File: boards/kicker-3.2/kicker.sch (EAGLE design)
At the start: 151 parts, among them J1 B2PS-VH(LF)(SN), J2 HFW8R-1ST, J3 B2PS-VH(LF)(SN), J4 B2PS-VH(LF)(SN), J5 2-PIN_2MM-H, J6 3-PIN_2MM-H, J7 !BTN_KCK_PRE_EXT, J8 !BTN_CHP_PRE_EXT, J9 !BTN_CHG_PRE_EXT, Q1 ATP302ATPAK, Q10 BSS806NSOT-23-3, Q2 IRFS4227, Q3 BSS127, Q4 BSS127, Q5 BSS127, Q6 BSS127, Q7 AOD1N60, T1 DA203X-ALDA2034, U1 MPM3620GQV-P, U2 15V, U3 LT3751FE, U4 AT32ATQFP44, U5 IX4427N, U6 MAX6817, U7 MAX6817

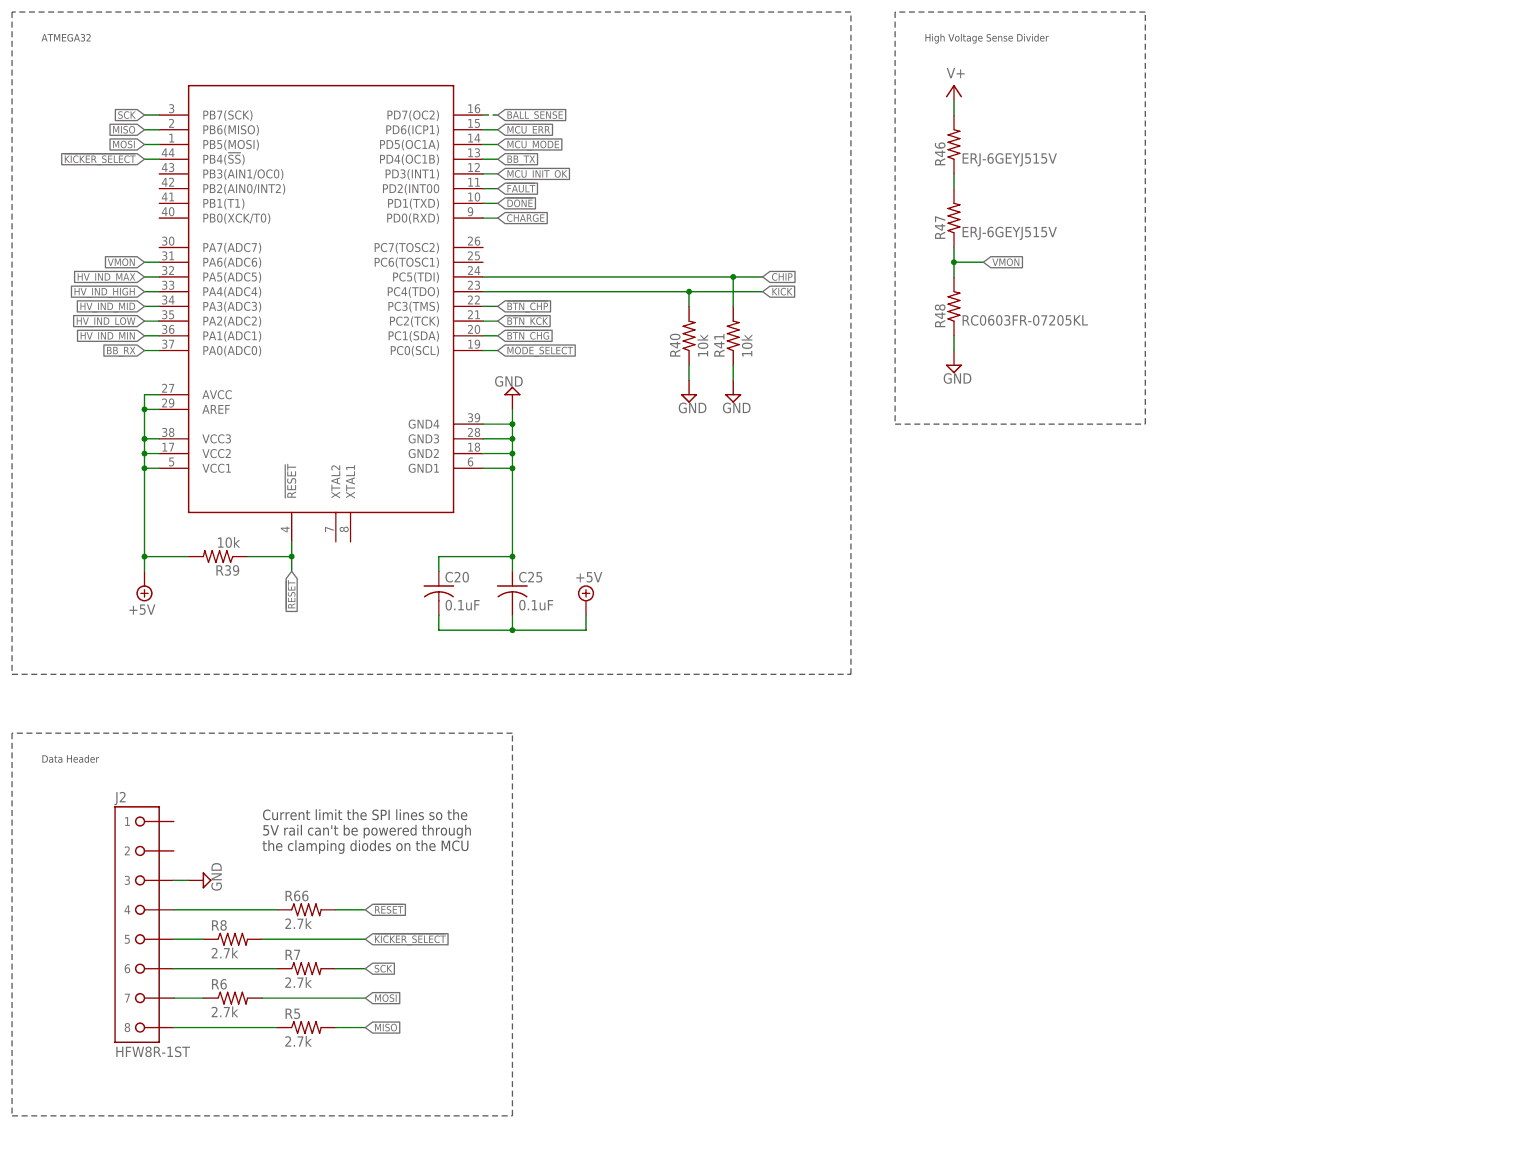
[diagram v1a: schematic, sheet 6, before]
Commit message: kicker passing initial drc checks
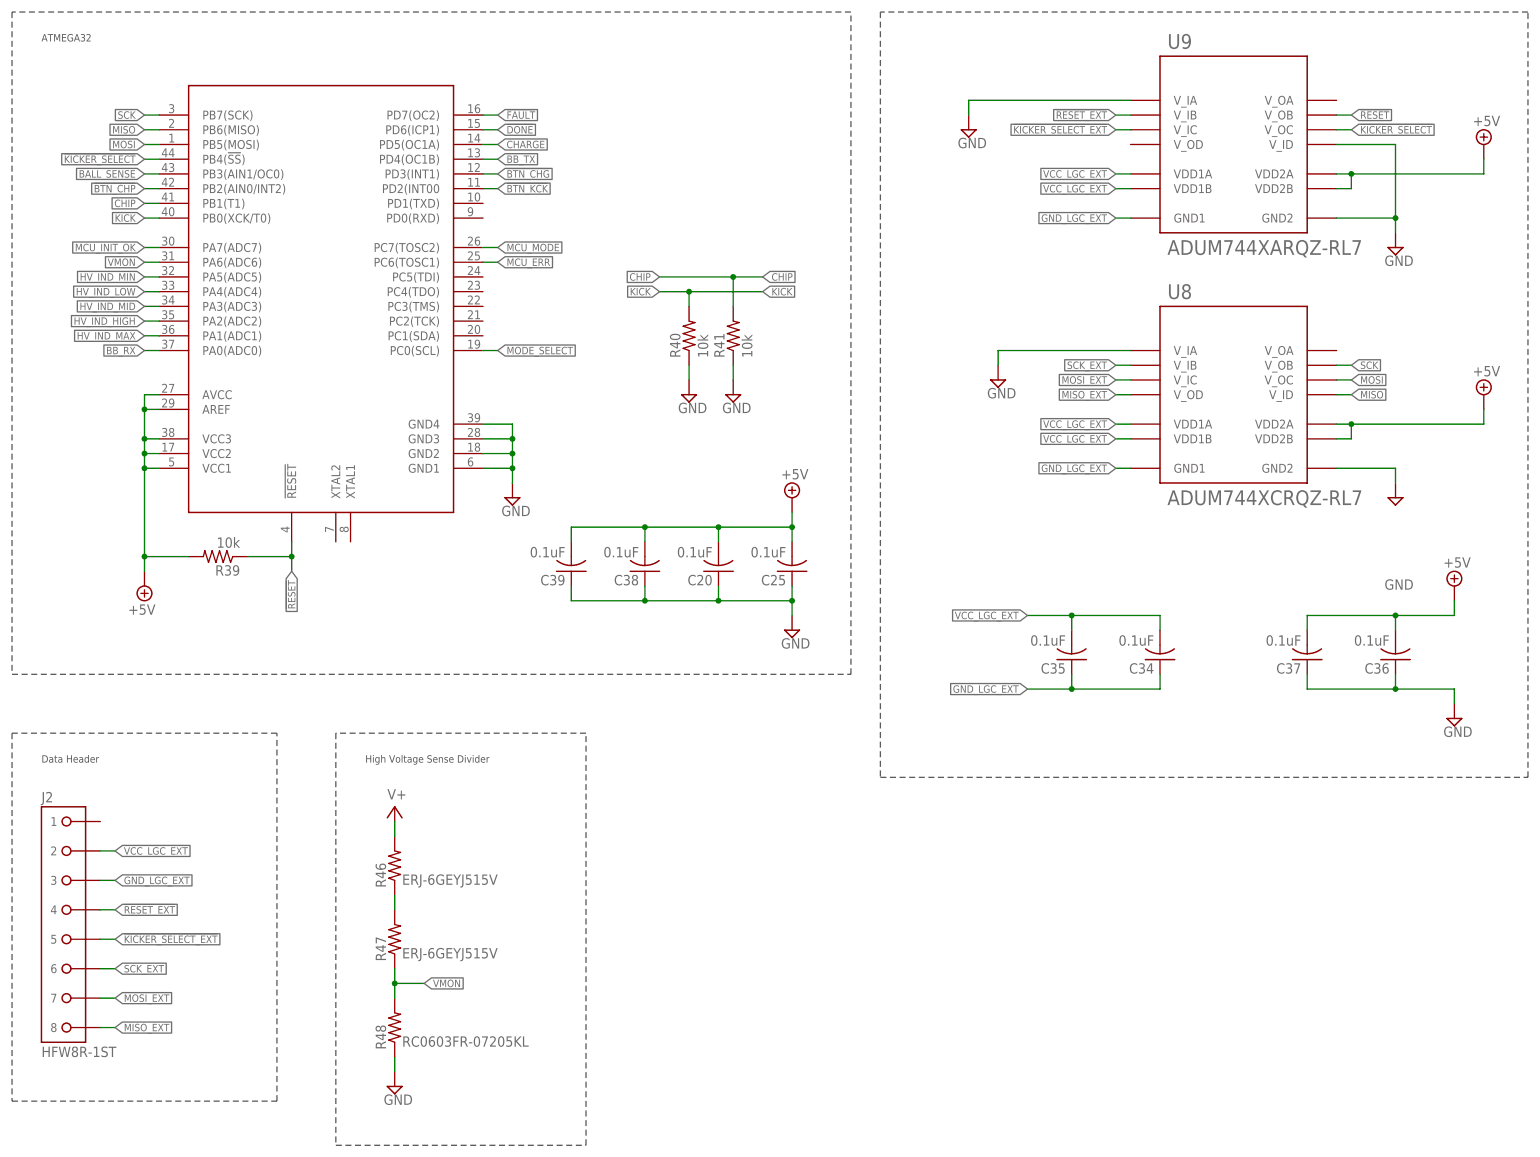
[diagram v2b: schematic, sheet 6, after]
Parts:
- removed R21, R23, R32: 162, rcl:R-US_R0603
- removed R25, R27, R29, R33: 261, rcl:R-US_R0603
- removed R5, R6, R66, R7, R8: 2.7k, resistor:R-US_R0603
- removed R55: 60, rcl:R-US_R0603
- removed U6, U7: MAX6817, RoboJackets-ICs:MAX6817
- added C34, C35, C36, C37, C38, C39: 0.1uF, rcl:C-USC0603
- added RN1: 330, RoboJackets-Resistors:RA-8
- added RV1: 500, RoboJackets-Resistors:PVG3
- added U8: ADUM744XCRQZ-RL7, RoboJackets-ICs:ADUM744XCRQZ-RL7
- added U9: ADUM744XARQZ-RL7, RoboJackets-ICs:ADUM744XARQZ-RL7
- R22, R24: value 162 -> 330
- R28: value 261 -> 330
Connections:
- removed net !BTN_CHG_PRE: J9.1, R53.1, S3.A2, U7.IN2
- removed net !BTN_CHP_PRE: J8.1, R52.1, S2.A2, U6.IN2
- removed net !BTN_KCK_PRE: J7.1, R54.1, S4.A2, U6.IN1
- removed net !KICKER_SELECT_CL: J2G$1.5, R8.1
- removed net !RESET_CL: J2G$1.4, R66.1
- removed net MISO_CL: J2G$1.8, R5.1
- removed net MOSI_CL: J2G$1.7, R6.1
- removed net N$11: D3.A, R21.1
- removed net N$12: D5.A, R23.1
- removed net N$13: D7.A, R25.1
- removed net N$17: D20.A, R55.1
- removed net N$21: D8.A, R27.1
- removed net N$30: D10.A, R29.1
- removed net N$4: D13.A, R32.1
- removed net N$40: D12.A, R31.1
- removed net SCK_CL: J2G$1.6, R7.1
- new net !KICKER_SELECT_EXT: J2G$1.5, U9.V_IC
- new net !RESET_EXT: J2G$1.4, U9.V_IB
- new net BALL_SENSE_CL: D12.K, R31.1
- new net GND_LGC_EXT: C34.1, C35.1, J2G$1.3, U8.GND1, U9.GND1
- new net HV_IND_HIGH_CL: D8.K, RN1.7
- new net HV_IND_LOW_CL: D5.K, RN1.5
- new net HV_IND_MAX_CL: D10.K, RN1.8
- new net HV_IND_MID_CL: D7.K, RN1.6
- new net HV_IND_MIN_CL: D3.K, RN1.4
- new net MCU_ERR_CL: D14.K, RN1.1
- new net MCU_INIT_OK_CL: D13.K, RN1.3
- new net MCU_MODE_CL: D20.K, RN1.2
- new net MISO_EXT: J2G$1.8, U8.V_OD
- new net MOSI_EXT: J2G$1.7, U8.V_IC
- new net N$2: U8.V_IA
- new net SCK_EXT: J2G$1.6, U8.V_IB
- new net VCC_LGC_EXT: C34.2, C35.2, J2G$1.2, U8.VDD1A, U8.VDD1B, U9.VDD1A, U9.VDD1B
- net !BTN_CHG: now also J9.1, R53.1, S3.A2, U4.PD3(INT1); no longer U4.PC1(SDA), U7.OUT2
- net !BTN_CHP: now also J8.1, R52.1, S2.A2, U4.PB2(AIN0/INT2); no longer U4.PC3(TMS), U6.OUT2
- net !BTN_KCK: now also J7.1, R54.1, S4.A2, U4.PD2(INT00; no longer U4.PC2(TCK), U6.OUT1
- net !DONE!: now also U4.PD6(ICP1); no longer U4.PD1(TXD)
- net !FAULT!: now also U4.PD7(OC2); no longer U4.PD2(INT00
- net !KICKER_SELECT: now also U9.V_OC; no longer R8.2
- net !RESET: now also U9.V_OB; no longer R66.2
- net +5V: now also C36.2, C37.2, C38.2, C39.2, D10.A, D12.A, D13.A, D14.A, D20.A, D3.A, D5.A, D7.A, D8.A, RV1.PIN2, U8.VDD2A, U8.VDD2B, U9.VDD2A, U9.VDD2B; no longer R21.2, R23.2, R25.2, R27.2, R29.2, R31.2, R32.2, R33.2, R49.1, R55.2, U6.VCC, U7.VCC
- net BALL_SENSE: now also R31.2, U4.PB3(AIN1/OC0); no longer D12.K, U4.PD7(OC2)
- net CHARGE: now also U4.PD5(OC1A); no longer U4.PD0(RXD)
- net CHIP: now also U4.PB1(T1); no longer U4.PC5(TDI)
- net GND: now also C36.1, C37.1, C38.1, C39.1, U8.GND2, U9.GND2, U9.V_IA, U9.V_ID; no longer J2G$1.3, U6.GND, U7.GND
- net HV_IND_HIGH: now also RN1.10, U4.PA2(ADC2); no longer D8.K, U4.PA4(ADC4)
- net HV_IND_LOW: now also RN1.12, U4.PA4(ADC4); no longer D5.K, U4.PA2(ADC2)
- net HV_IND_MAX: now also RN1.9, U4.PA1(ADC1); no longer D10.K, U4.PA5(ADC5)
- net HV_IND_MID: now also RN1.11; no longer D7.K
- net HV_IND_MIN: now also RN1.13, U4.PA5(ADC5); no longer D3.K, U4.PA1(ADC1)
- net KICK: now also U4.PB0(XCK/T0); no longer U4.PC4(TDO)
- net MCU_ERR: now also RN1.16, U4.PC6(TOSC1); no longer D14.K, U4.PD6(ICP1)
- net MCU_INIT_OK: now also RN1.14, U4.PA7(ADC7); no longer D13.K, U4.PD3(INT1)
- net MCU_MODE: now also RN1.15, U4.PC7(TOSC2); no longer D20.K, U4.PD5(OC1A)
- net MISO: now also U8.V_ID; no longer R5.2
- net MOSI: now also U8.V_OC; no longer R6.2
- net N$3: now also R49.1, RV1.PIN3; no longer D14.A, R33.1
- net SCK: now also U8.V_OB; no longer R7.2
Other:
- note removed: "Charge Switch"
- note removed: "Current limit the SPI lines so the 5V rail can't be powered through the clamping diodes on the MCU"
- note removed: "MCU Status"
- note removed: "Mode"
- moved on the sheet: C20, C25, D10, D12, D13, D14, D20, D3, D5, D7, D8, J2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

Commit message: updated LT calibration, added docs for LT
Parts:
- removed D24: PTVS20VS1UR, RoboJackets-Diodes:TVSSOD123W
- removed R53, R54: 10k, rcl:R-US_R0603
- removed R56: 22, resistor:R-US_R0805
- removed R57: 100k, rcl:R-US_R0603
- removed R59: 100k, rcl:R-US_R0402
- removed R60: 43.2k, rcl:R-US_R0603
- removed R61: 160k 1%, rcl:R-US_R0402
- removed R62: 30.1k 1%, rcl:R-US_R0402
- removed R64: 931, rcl:R-US_R0805
- removed R65: 160, rcl:R-US_R0603
- removed U$6, U$7: IXGK400N30A3, RoboJackets-Discrete:IXGK400N30A3
- added D21: BLUE, RoboJackets-LEDs:LED-SMD-BLUE
- added Q8, Q9: BSS127, RoboJackets-Discrete:BSS127
- added R23: 100k, rcl:R-US_R0603
- added R25: 10k, rcl:R-US_R0603
- added R27: 160, rcl:R-US_R1206
- added R29: 270k, rcl:R-US_R0603
- added R32: ERJ-6GEYJ515V, rcl:R-US_R0805
- added R33: 1.5k 35W, RoboJackets-Resistors:PWR263S-35TO-263AB
- added R5: 110k 1%, resistor:R-US_R0603
- added R6: 10k 1%, resistor:R-US_R0603
- added R7: 294k 1%, resistor:R-US_R0805
- added R8: 412k 1%, resistor:R-US_R0805
- C11: value 560uF -> 10uF (X7R); device rcl:CPOL-USE7.5-18 -> rcl:C-USC1210
- C12: value 1000uF -> 10uF (X7R); device rcl:CPOL-USE10-25 -> rcl:C-USC1210
- C13, C27: value 0.1uF -> 10uF (X7R); device rcl:C-USC0603 -> rcl:C-USC1210
- C14: value 1000uF -> 0.1uF; device rcl:CPOL-USE10-25 -> rcl:C-USC0603
- C15: value 10pF -> 0.1uF; device resistor:C-USC0603 -> rcl:C-USC0603
- C16, C32, C33: value 10uF (X7R) -> 0.1uF; device rcl:C-USC1210 -> rcl:C-USC0603
- C17, C18: value 10uF (X7R) -> 10pF; device rcl:C-USC1210 -> resistor:C-USC0603
- C19: value 10uF (X7R) -> 1uF; device rcl:C-USC1210 -> rcl:C-USC0603
- C20, C25: value 0.1uF -> 1uF
- C21: value 0.1uF 35V -> 560uF; device rcl:C-USC0603 -> rcl:CPOL-USE7.5-18
- C22: value 22uF 35V -> 10uF (X7R); device rcl:C-USC0805 -> rcl:C-USC1210
- C23, C24: value 0.1uF 50V -> 10uF (X7R); device rcl:C-USC0603 -> rcl:C-USC1210
- C26: value 220pF 100V -> 10uF (X7R); device resistor:C-USC0805 -> rcl:C-USC1210
- C28: value 0.1uF -> 0.1uF 35V
- C29: value 10pF -> 22uF 35V; device resistor:C-USC0603 -> rcl:C-USC0805
- C30, C31: value 10uF (X7R) -> 0.1uF 50V; device rcl:C-USC1210 -> rcl:C-USC0603
- C4: value 1uF -> 2.2uF
- C5: value 1uF -> 1000uF; device rcl:C-USC0603 -> rcl:CPOL-USE10-25
- C6: value 2.2uF -> 1000uF; device rcl:C-USC0603 -> rcl:CPOL-USE10-25
- C9: value 1uF -> 220pF 100V; device rcl:C-USC0603 -> resistor:C-USC0805
- D1: value VS-5EWH06FN-M3D-PAK_TO252AA -> PTVS20VS1UR; device RoboJackets-Diodes:VS-5EWH06FN-M3D-PAK_TO252AA -> RoboJackets-Diodes:TVSSOD123W
- D10, D8: value RED -> GREEN; device RoboJackets-LEDs:LED-SMD-RED -> RoboJackets-LEDs:LED-SMD-GREEN
- D11: value YELLOW -> RED; device RoboJackets-LEDs:LED-SMD-YELLOW -> RoboJackets-LEDs:LED-SMD-RED
- D12: value BLUE -> YELLOW; device RoboJackets-LEDs:LED-SMD-BLUE -> RoboJackets-LEDs:LED-SMD-YELLOW
- D13: value GREEN -> YELLOW; device RoboJackets-LEDs:LED-SMD-GREEN -> RoboJackets-LEDs:LED-SMD-YELLOW
- D14: value RED -> BLUE; device RoboJackets-LEDs:LED-SMD-RED -> RoboJackets-LEDs:LED-SMD-BLUE
- D15: value 3SMBJ5929B-TP -> GREEN; device RoboJackets-Diodes:DIODE-DO214AA -> RoboJackets-LEDs:LED-SMD-GREEN
- D16: value SMAJ20ADO-214AC -> GREEN; device RoboJackets-Diodes:SMAJ20ADO-214AC -> RoboJackets-LEDs:LED-SMD-GREEN
- D17: value SMAJ20ADO-214AC -> YELLOW; device RoboJackets-Diodes:SMAJ20ADO-214AC -> RoboJackets-LEDs:LED-SMD-YELLOW
- D18, D19: value VS-5EWH06FN-M3D-PAK_TO252AA -> RED; device RoboJackets-Diodes:VS-5EWH06FN-M3D-PAK_TO252AA -> RoboJackets-LEDs:LED-SMD-RED
- D2, D6: value GREEN -> VS-5EWH06FN-M3D-PAK_TO252AA; device RoboJackets-LEDs:LED-SMD-GREEN -> RoboJackets-Diodes:VS-5EWH06FN-M3D-PAK_TO252AA
- D3: value BLUE -> SMAJ20ADO-214AC; device RoboJackets-LEDs:LED-SMD-BLUE -> RoboJackets-Diodes:SMAJ20ADO-214AC
- D4: value GREEN -> SMAJ20ADO-214AC; device RoboJackets-LEDs:LED-SMD-GREEN -> RoboJackets-Diodes:SMAJ20ADO-214AC
- D5: value YELLOW -> VS-5EWH06FN-M3D-PAK_TO252AA; device RoboJackets-LEDs:LED-SMD-YELLOW -> RoboJackets-Diodes:VS-5EWH06FN-M3D-PAK_TO252AA
- D7: value YELLOW -> 3SMBJ5929B-TP; device RoboJackets-LEDs:LED-SMD-YELLOW -> RoboJackets-Diodes:DIODE-DO214AA
- J2: value HFW8R-1ST -> B2PS-VH(LF)(SN); device RoboJackets-Connectors:HFW8R-1ST -> RoboJackets-Connectors:B2PS-VH(LF)(SN)
- J4: value B2PS-VH(LF)(SN) -> HFW8R-1ST; device RoboJackets-Connectors:B2PS-VH(LF)(SN) -> RoboJackets-Connectors:HFW8R-1ST
- Q3, Q4: value BSS127 -> IXGK400N30A3; device RoboJackets-Discrete:BSS127 -> RoboJackets-Discrete:IXGK400N30A3
- Q6: value BSS127 -> AOD1N60; device RoboJackets-Discrete:BSS127 -> RoboJackets-Discrete:AOD1N60
- Q7: value AOD1N60 -> BSS127; device RoboJackets-Discrete:AOD1N60 -> RoboJackets-Discrete:BSS127
- R1: value 110k 1% -> 43.2k; device resistor:R-US_R0603 -> rcl:R-US_R0603
- R11: value 294k 1% -> 25,5k 1%
- R12: value 412k 1% -> 1.00k 1%
- R13: value 40.2k 1% -> 11.5k 1%
- R14: value 1.62k 1% -> 25.5k 1%
- R15: value 18.2k 1% -> 22
- R16: value 40.2k 1% -> 15m 1%; device resistor:R-US_R0805 -> resistor:R-US_R2512
- R18: value 15m 1% -> 931; device resistor:R-US_R2512 -> rcl:R-US_R0805
- R2: value 10k 1% -> 100k; device resistor:R-US_R0603 -> rcl:R-US_R0402
- R20: value 1k -> 100k
- R22, R24: value 330 -> 160
- R26: value 1k -> 10k
- R28: value 330 -> 160; device rcl:R-US_R0603 -> rcl:R-US_R1206
- R3: value 160 -> 160k 1%; device rcl:R-US_R0603 -> rcl:R-US_R0402
- R30: value ERJ-P06J274V -> 100k; device rcl:R-US_R0805 -> rcl:R-US_R0603
- R31: value 60 -> ERJ-6GEYJ515V; device rcl:R-US_R0603 -> rcl:R-US_R0805
- R34: value 270k -> 10k
- R35: value 100k -> ERJ-6GEYJ515V; device rcl:R-US_R0603 -> rcl:R-US_R0805
- R37: value ERJ-6GEYJ515V -> RC0603FR-07205KL; device rcl:R-US_R0805 -> rcl:R-US_R0603
- R38: value 1.5k 35W -> 10k; device RoboJackets-Resistors:PWR263S-35TO-263AB -> rcl:R-US_R0603
- R4: value 100k -> 30.1k 1%; device rcl:R-US_R0603 -> rcl:R-US_R0402
- R40, R43: value 10k -> 1k
- R41, R42: value 10k -> 330
- R44: value 160 -> 330; device rcl:R-US_R1206 -> rcl:R-US_R0603
- R45: value 160 -> ERJ-P06J274V; device rcl:R-US_R1206 -> rcl:R-US_R0805
- R46: value ERJ-6GEYJ515V -> 60; device rcl:R-US_R0805 -> rcl:R-US_R0603
- R47: value ERJ-6GEYJ515V -> 50; device rcl:R-US_R0805 -> rcl:R-US_R0603
- R48: value RC0603FR-07205KL -> 10k
- R49: value 50 -> 10k
- U4: value AT32ATQFP44 -> IX4427N; device RoboJackets-ICs:AT32ATQFP44 -> RoboJackets-PowerICs:IX4427N
- U5: value IX4427N -> AT32ATQFP44; device RoboJackets-PowerICs:IX4427N -> RoboJackets-ICs:AT32ATQFP44
- XF1: value 30A -> 20A
- renumbered R58 to R21, R63 to R17, U8 to U7, U9 to U6
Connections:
- net !BTN_CHG: now also R52.1, S4.A2, U5.PD3(INT1); no longer R53.1, S3.A2, U4.PD3(INT1)
- net !BTN_CHP: now also R50.1, U5.PB2(AIN0/INT2); no longer R52.1, U4.PB2(AIN0/INT2)
- net !BTN_KCK: now also R51.1, S3.A2, U5.PD2(INT00; no longer R54.1, S4.A2, U4.PD2(INT00
- net !DONE!: now also C19.1, U5.PD6(ICP1); no longer C4.1, U4.PD6(ICP1)
- net !DONE!_RAW: now also Q7.G; no longer Q3.G
- net !FAULT!: now also C20.1, R22.1, U5.PD7(OC2); no longer C3.1, R65.1, U4.PD7(OC2)
- net !FAULT!_RAW: now also Q8.G, R20.1, R22.2; no longer Q4.G, R57.1, R65.2
- net !KICKER_SELECT: now also U5.PB4(!SS!); no longer U4.PB4(!SS!)
- net !KICKER_SELECT_EXT: now also J4G$1.5; no longer J2G$1.5
- net !RESET: now also R34.1, U5.!RESET!; no longer R39.1, U4.!RESET!
- net !RESET_EXT: now also J4G$1.4; no longer J2G$1.4
- net +15.0V: now also C28.2, C29.2, C4.1, R40.2, R5.2, U4.VDD; no longer C21.2, C22.2, C6.1, R1.2, R20.2, U5.VDD
- net +5V: now also C32.2, C33.2, C34.2, C35.2, D11.A, D16.A, D17.A, D18.A, D21.A, D9.A, R20.2, R3.2, R34.2, R41.2, R42.2, R43.2, R44.2, R48.2, R51.2, U5.AREF, U5.AVCC, U5.VCC1, U5.VCC2, U5.VCC3; no longer C20.2, C25.2, C36.2, C37.2, D10.A, D20.A, D3.A, D5.A, D7.A, D8.A, R22.2, R24.2, R26.2, R28.2, R39.2, R53.2, R54.2, R57.2, R61.2, U4.AREF, U4.AVCC, U4.VCC1, U4.VCC2, U4.VCC3
- net 15V_PWR_BR: now also D8.A, R40.1; no longer D2.A, R20.1
- net BALL_SENSE: now also R46.2, U5.PB3(AIN1/OC0); no longer R31.2, U4.PB3(AIN1/OC0)
- net BALL_SENSE_CL: now also D21.K, R46.1; no longer D12.K, R31.1
- net BB_RX: now also R48.1, U5.PA0(ADC0); no longer R50.1, U4.PA0(ADC0)
- net BB_TX: now also U5.PD4(OC1B); no longer U4.PD4(OC1B)
- net BB_TX_CL: now also R47.2; no longer R49.2
- net CHARGE: now also C25.1, R24.1, U5.PD5(OC1A); no longer C9.1, R3.1, U4.PD5(OC1A)
- net CHARGE_RAW: now also R23.2, R24.2; no longer R3.2, R4.2
- net CHIP: now also R39.2, U4.IN_A, U5.PB1(T1); no longer R41.2, U4.PB1(T1), U5.IN_A
- net CHIPPER: now also D5.A, J2.2, Q3.C; no longer D18.A, J3.2, U$7.C
- net CHIP_GATE: now also R25.2, R27.1, U4.OUT_A; no longer R42.2, R44.1, U5.OUT_A
- net CHIP_GATE_S: now also C30.1, D3.C, Q3.G, R27.2; no longer C23.1, D16.C, R44.2, U$7.G
- net CSP: now also R16.2; no longer R18.2
- net DISCHARGE_DRAIN: now also D20.K, Q6.D, R33.PIN2; no longer D11.K, Q7.D, R38.PIN2
- net FAULT_INV_BR: now also Q8.D, Q9.G, R43.1; no longer Q4.D, Q5.G, R26.1
- net FB: now also R3.1, R4.2; no longer R61.1, R62.2
- net GND: now also C11.2, C12.2, C14.2, C20.2, C21.-, C22.2, C25.2, C26.2, C28.1, C29.1, C32.1, C33.1, C34.1, C35.1, C5.-, C6.-, D1.A, D10.K, D3.A, D4.A, D7.A, D8.K, Q3.E, Q4.E, Q8.S, Q9.S, R1.1, R12.2, R16.1, R18.2, R23.1, R25.1, R26.1, R30.1, R37.1, R38.1, R39.1, R6.1, U4.GND, U5.GND1, U5.GND2, U5.GND3, U5.GND4; no longer C11.-, C12.-, C14.-, C20.1, C21.1, C22.1, C25.1, C28.2, C29.2, C32.2, C33.2, C36.1, C37.1, C5.2, C6.2, C9.2, D15.A, D16.A, D17.A, D2.K, D24.A, D4.K, Q3.S, Q4.S, R14.2, R18.1, R2.1, R35.1, R40.1, R41.1, R42.1, R43.1, R48.1, R60.1, R62.1, R64.2, U$6.E, U$7.E, U4.GND1, U4.GND2, U4.GND3, U4.GND4, U5.GND
- net GND_LGC_EXT: now also C36.1, C37.1, J4G$1.3; no longer C34.1, C35.1, J2G$1.3
- net HV_AC: now also D2.A; no longer D1.A
- net HV_FB: now also R18.1; no longer R64.1
- net HV_IND_HIGH: now also U5.PA2(ADC2); no longer U4.PA2(ADC2)
- net HV_IND_HIGH_CL: now also D11.K; no longer D8.K
- net HV_IND_LOW: now also U5.PA4(ADC4); no longer U4.PA4(ADC4)
- net HV_IND_LOW_CL: now also D13.K; no longer D5.K
- net HV_IND_MAX: now also U5.PA1(ADC1); no longer U4.PA1(ADC1)
- net HV_IND_MAX_CL: now also D9.K; no longer D10.K
- net HV_IND_MID: now also U5.PA3(ADC3); no longer U4.PA3(ADC3)
- net HV_IND_MID_CL: now also D12.K; no longer D7.K
- net HV_IND_MIN: now also U5.PA5(ADC5); no longer U4.PA5(ADC5)
- net HV_IND_MIN_CL: now also D14.K; no longer D3.K
- net HV_SENSE_DIV_BR: now also R35.1, R36.2; no longer R46.1, R47.2
- net KICK: now also R38.2, U4.IN_B, U5.PB0(XCK/T0); no longer R40.2, U4.PB0(XCK/T0), U5.IN_B
- net KICKER: now also D6.A, J3.1, Q4.C; no longer D19.A, J4.1, U$6.C
- net KICK_GATE: now also R26.2, R28.1, U4.OUT_B; no longer R43.2, R45.1, U5.OUT_B
- net KICK_GATE_S: now also C31.1, D4.C, Q4.G, R28.2; no longer C24.1, D17.C, R45.2, U$6.G
- net MCU_ERR: now also U5.PC6(TOSC1); no longer U4.PC6(TOSC1)
- net MCU_ERR_CL: now also D18.K; no longer D14.K
- net MCU_INIT_OK: now also U5.PA7(ADC7); no longer U4.PA7(ADC7)
- net MCU_INIT_OK_CL: now also D16.K; no longer D13.K
- net MCU_MODE: now also U5.PC7(TOSC2); no longer U4.PC7(TOSC2)
- net MCU_MODE_CL: now also D17.K; no longer D20.K
- net MISO: now also U5.PB6(MISO); no longer U4.PB6(MISO)
- net MISO_EXT: now also J4G$1.8; no longer J2G$1.8
- net MODE_SELECT: now also R49.2, U5.PC0(SCL); no longer R51.2, U4.PC0(SCL)
- net MOSI: now also U5.PB5(MOSI); no longer U4.PB5(MOSI)
- net MOSI_EXT: now also J4G$1.7; no longer J2G$1.7
- net N$1: now also R12.1; no longer R14.1
- net N$14: now also R49.1; no longer R51.1
- net N$16: now also R5.1, R6.2; no longer R1.1, R2.2
- net N$18: now also C9.1, R15.2; no longer C26.1, R56.2
- net N$20: now also D10.A, R41.1; no longer D4.A, R22.1
- net N$24: now also R11.1; no longer R13.1
- net N$27: now also D19.A, R44.1; no longer D9.A, R28.1
- net N$28: now also D19.K, Q9.D; no longer D9.K, Q5.D
- net N$29: now also D20.A, R45.1; no longer D11.A, R30.1
- net N$3: now also R47.1; no longer R49.1
- net N$37: now also D15.K, Q7.D; no longer D6.K, Q3.D
- net N$5: now also D15.A, R42.1; no longer D6.A, R24.1
- net OVLO1: now also R8.2; no longer R10.2
- net OVLO2: now also R10.2; no longer R12.2
- net QD_GATE_CTRL: now also Q5.G, R29.1, R30.2; no longer Q6.G, R34.1, R35.2
- net QD_PU_BR: now also R31.1, R32.2; no longer R36.1, R37.2
- net QUICK_DISCHARGE: now also D7.C, Q5.D, Q6.G, R32.1; no longer D15.C, Q6.D, Q7.G, R37.1
- net RDCM: now also R13.2; no longer R15.2
- net REG_AAM: now also R1.2; no longer R60.2
- net REG_EN: now also R2.2; no longer R59.2
- net RVOUT: now also R14.2; no longer R16.2
- net SCK: now also U5.PB7(SCK); no longer U4.PB7(SCK)
- net SCK_EXT: now also J4G$1.6; no longer J2G$1.6
- net UVLO1: now also R7.2; no longer R9.2
- net UVLO2: now also R9.2; no longer R11.2
- net V+: now also C5.+, C6.+, D2.C, D5.C, D6.C, J2.1, J3.2, R31.2, R33.PIN1, R35.2, R45.2; no longer C12.+, C14.+, D1.C, D18.C, D19.C, J3.1, J4.2, R30.2, R36.2, R38.PIN1, R46.2
- net VBATT: now also C11.1, C12.1, C14.1, C21.+, C22.1, C23.1, C24.1, C26.1, C3.1, C9.2, D1.C, R11.2, R2.1, R29.2, R7.1, R8.1; no longer C11.+, C19.1, C26.2, C28.1, C29.1, C30.1, C31.1, C32.1, C33.1, C5.1, D24.C, R11.1, R12.1, R13.2, R34.2, R59.1
- net VCC_LGC_EXT: now also C36.2, C37.2, J4G$1.2; no longer C34.2, C35.2, J2G$1.2
- net VMON: now also R36.1, R37.2, U5.PA6(ADC6); no longer R47.1, R48.2, U4.PA6(ADC6)
- net VSN: now also R13.1, R14.1; no longer R16.1, R56.1
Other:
- note added: "(opt) 0ohm"
- note added: "Avoid JTAG pins"
- note added: "Current Limit: I = 106mV / Rshunt I = 0.106/0.015 = 7.06A I = 0.106/0.011 = 9.63A I = 0.106/0.010 = 10.6A Power Dissipation: P = I^2 x R P = (7.066^2)*0.015 = 0.7489W P = (10.6^2)*0.015 = 1.6854W"
- note added: "D2: Vfwd = 1.85 Trr = 18ns Trr_ideal @ Fsw=1MHz <= 10ns Trr_ideal @ Fsw=300KHz <= 33ns Trr_ideal @ Fsw=100KHz <= 100ns Fsw = 1 / (Ipk*Lpri*((1/Vtrans)+(N/Vout))) Fsw = 1 / (10*0.000010*((1/15.5)+(10/250))) Fsw = 1 / (10*0.000010*((1/21.5)+(10/250))) Fsw = 95.9kHz:115kHz"
- note added: "Desolder R17 and jump R18 to enter capacitor charging mode. This is recommended."
- note added: "Rbg = 0.98*N*(RVout / (RVout,trip + Vdiode)) Rbg = 0.98*10*(25500 / 251.8) Rbg = 992.45 ~ 1k (E96)"
- note added: "Req: Lparasitic < 2nH"
- note added: "Vdrain = Vtrans + (Vout + Vdiode) / N Vtrans = 15.5:21.5 Vdrain = 40.5:47.5 Vtrans RANGE = 6.0V DEL Vdrain RANGE (Vdrain - Vtrans) DEL Vdrain RANGE = 25.0:26.0 Table 2 (pg. 17): ENT: 4.75-60.0, 2.5-50.0"
- note added: "Vout = 250V Vtrans = 15.5:21.5 N <= Vout / Vtrans N <= 16.1:11.6 N = 10"
- note removed: "Too many notes to put in the schematic... see the accompanying design doc for the spec on this subsystem."

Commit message: kicker dr fixes
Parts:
- removed C17, C18: 10pF, resistor:C-USC0603
- C10, C11, C12, C13: value 10uF (X7R) -> 10uF (X7R) 35V
- C14, C15, C16: value 0.1uF -> 0.1uF 35V
- C3: value 1uF -> 1uF 50V
- C4: value 2.2uF -> 2.2uF 35V
- D2, D5, D6: value VS-5EWH06FN-M3D-PAK_TO252AA -> VS-5EWH06FN-M3
- D3, D4: value SMAJ20ADO-214AC -> SMAJ20A
- R1: value 43.2k -> 43.2k 1%
- R11: value 25,5k 1% -> 25.5k 1%
- R16: value 15m 1% -> 15m 1% >0.5W
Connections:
- net GND: no longer C17.2, C18.2
- net VBATT: no longer C17.1, C18.1
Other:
- note added: "AAM R1 and Voltage Divider selected from datasheet"
- note removed: "AAM R60 and Voltage Divider selected from datasheet"
- moved on the sheet: C12, C13, C14, C15, C16
